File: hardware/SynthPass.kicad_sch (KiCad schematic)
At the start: 14 parts, among them J1 SM04B-SRSS-TB, P1 USB_C_Plug_USB2.0, SW1 SW_Push, U2 CH572D, Y2 32MHz

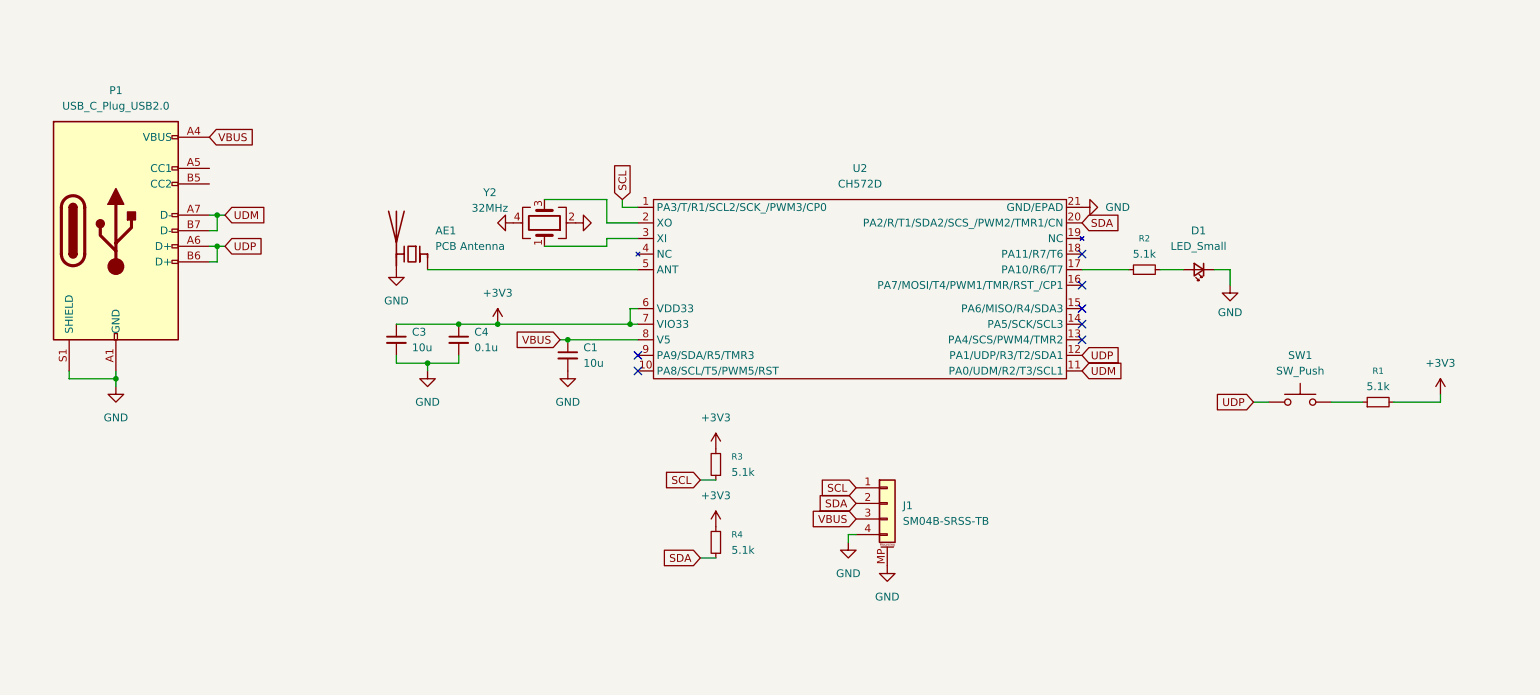
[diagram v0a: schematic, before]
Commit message: Change CH572 symbol, change UDP resistor to 1K5, add 1K5 5V->3V3 resistor
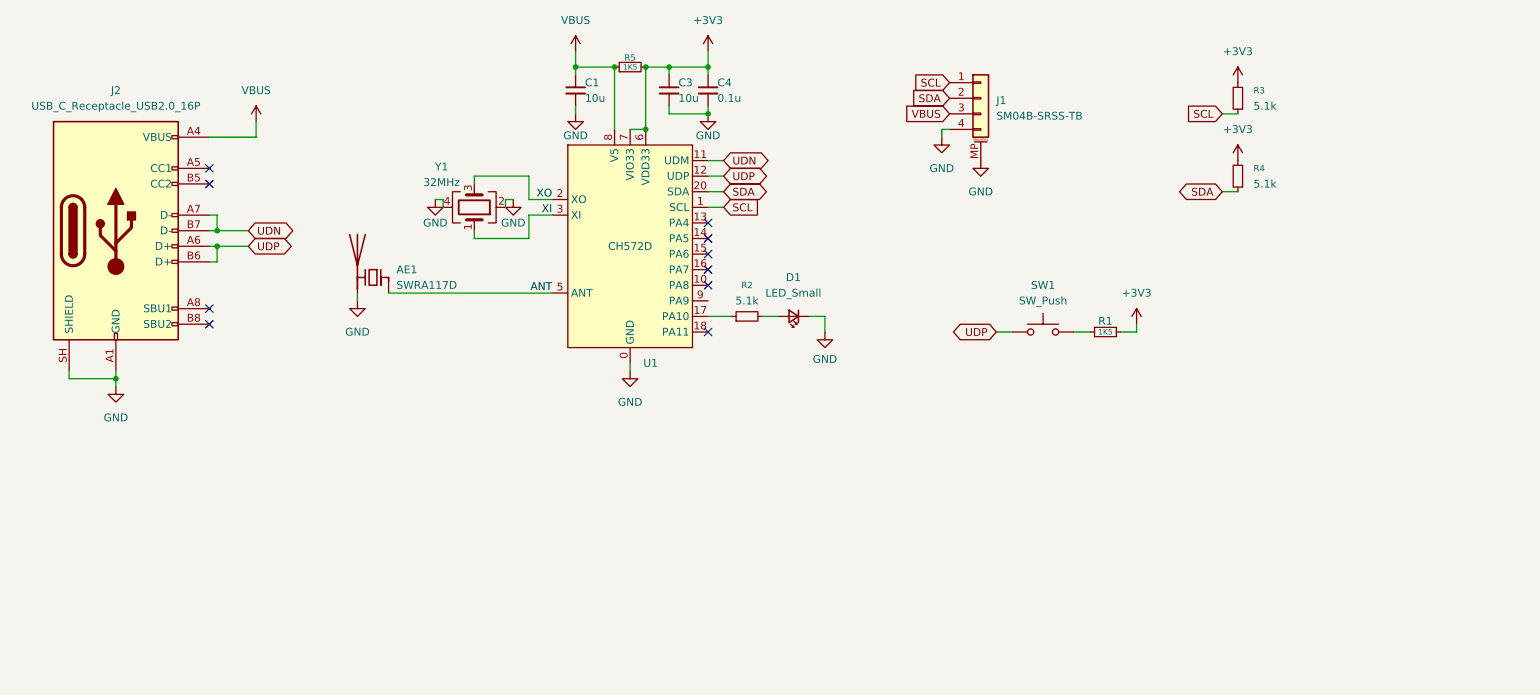
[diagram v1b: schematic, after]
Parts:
- removed U2: CH572D, CH572D:CH572D, symbol CH572D:CH572D
- removed Y2: 32MHz, Crystal:Crystal_SMD_3225-4Pin_3.2x2.5mm, symbol Device:Crystal_GND24
- added R5: 1K5, Resistor_SMD:R_0402_1005Metric, symbol Device:R_Small
- added U1: CH572D, CH572D:CH572D_New, symbol CH572D:CH572D_small
- added Y1: 32MHz, Crystal:Crystal_SMD_3225-4Pin_3.2x2.5mm, symbol Device:Crystal_GND24
- AE1: value PCB Antenna -> SWRA117D; now left out of the parts list
- J1: LCSC (none) -> C160404
- J2: renamed from P1; value USB_C_Plug_USB2.0 -> USB_C_Receptacle_USB2.0_16P; symbol Connector:USB_C_Receptacle_USB2.0_14P -> Connector:USB_C_Receptacle_USB2.0_16P; LCSC (none) -> C2988369
- R1: value 5.1k -> 1K5
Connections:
- net +3V3: now also R5.2, U1.6 (VDD33), U1.7 (VIO33)
- net GND: now also J2.SH (SHIELD), U1.0 (GND), Y1.2, Y1.4; no longer J2.S1 (SHIELD)
- net SCL: now also U1.1 (PA3)
- net SDA: now also U1.20 (PA2)
- net UDP: now also U1.12 (PA1)
- net VBUS: now also R5.1, U1.8 (V5)
- net at R2.1: now also U1.17 (PA10)
- net ANT: now reaches AE1.1 (FEED)
- net ANT: now also U1.5 (ANT)
- net UDM renamed UDN
- net UDN: now also U1.11 (PA0)
- new net: U1.19 (NC), U1.4 (NC)
- new net XI: U1.3 (XI), Y1.1
- new net XO: U1.2 (XO), Y1.3
- no-connect marks 7 -> 10
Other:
- moved on the sheet: J1, R1, R3, R4, SW1

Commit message: Add rev. # to schematic
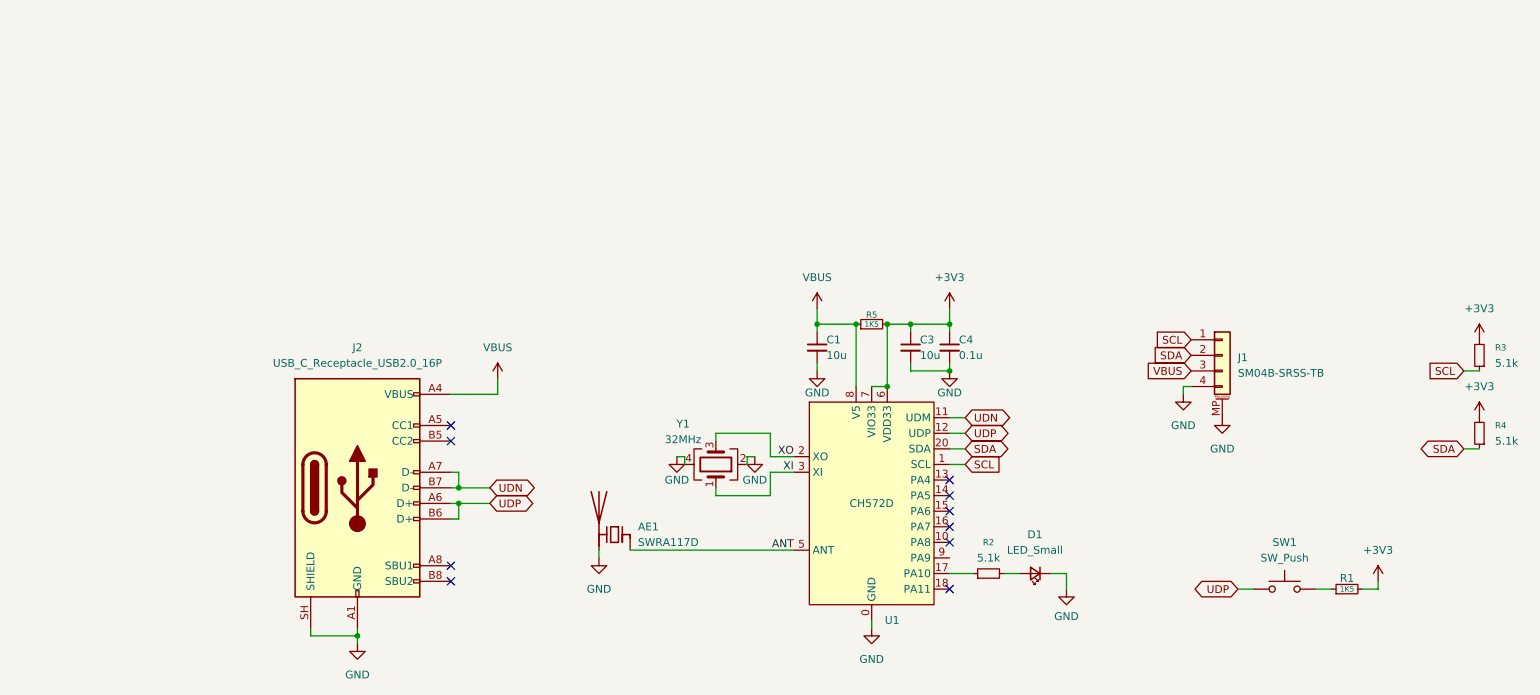
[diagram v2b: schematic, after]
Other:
- title: (none) -> Synthpass
- moved on the sheet: AE1, C1, C3, C4, D1, J1, J2, R1, R2, R3, R4, R5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
